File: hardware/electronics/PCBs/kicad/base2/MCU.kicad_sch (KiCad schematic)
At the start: 25 parts, among them J1 HEADER2, U1 W25Q16JVSSIQ, U6 RP2350A, Y1 ABM8-272-T3

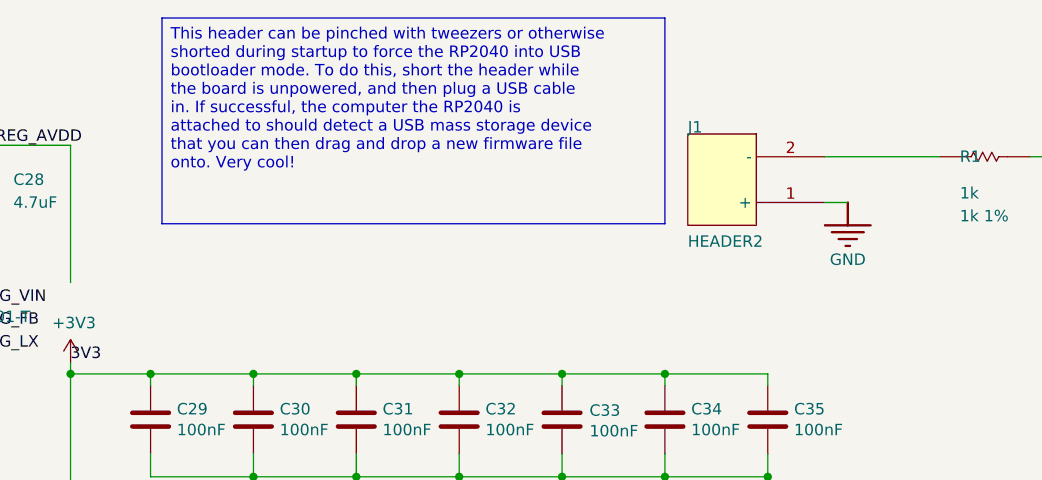
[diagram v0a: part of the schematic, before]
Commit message: Vertical neopixels
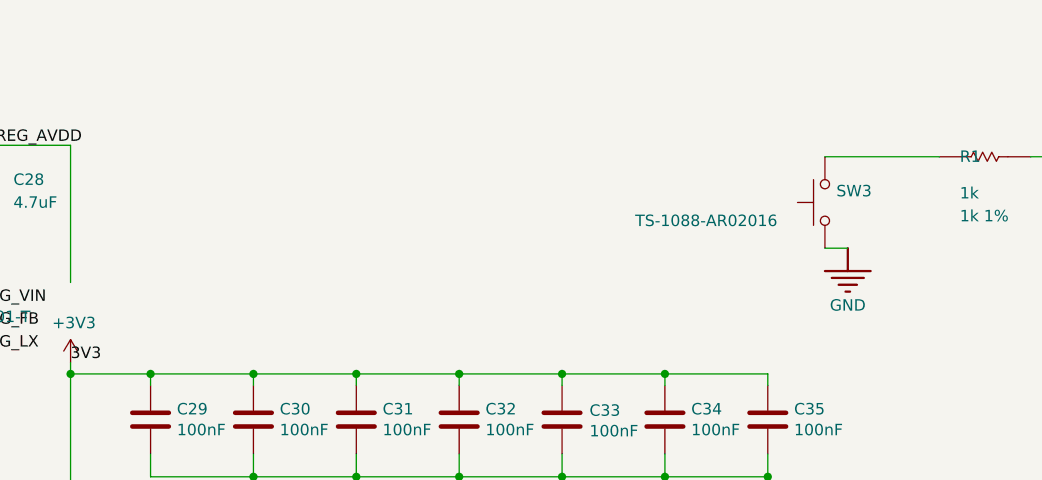
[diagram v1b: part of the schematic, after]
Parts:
- removed J1: HEADER2, 2x1, symbol Connectors:MCU_2_HEADER2_Connectors.SchLib
- added SW3: TS-1088-AR02016, Button_Switch_SMD:SW_SPST_TS-1088-xR020, symbol Switch:SW_Push
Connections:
- net GND: now also SW3.1
- net at R1.1: now also SW3.2
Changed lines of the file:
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@@
-		)
-	)
-	(text_box "This header can be pinched with tweezers or otherwise shorted during startup to force the RP2040 into USB bootloader mode. To do this, short the header while the board is unpowered, and then plug a USB cable in. If successful, the computer the RP2040 is attached to should detect a USB mass storage device that you can then drag and drop a new firmware file onto. Very cool!"
-		(exclude_from_sim no)
-		(at 167.64 65.8622 0)
-		(size -55.88 22.86)
-		(margins 0.9525 0.9525 0.9525 0.9525)
-		(stroke
-			(width 0)
-			(type default)
-			(color 0 0 0 1)
-		)
-		(fill
-			(type color)
-			(color 255 255 255 1)
-		)
-		(effects
-			(font
-				(size 1.27 1.27)
-			)
-			(justify left top)
 		)
 	)
@@
 	(wire
 		(pts
-			(xy 187.96 86.36) (xy 185.42 86.36)
+			(xy 187.96 91.44) (xy 185.42 91.44)
 		)
 		(stroke
@@
 	)
 	(symbol
+		(lib_id "Switch:SW_Push")
+		(at 185.42 86.36 90)
+		(unit 1)
+		(body_style 1)
+		(exclude_from_sim no)
+		(in_bom yes)
+		(on_board yes)
+		(in_pos_files yes)
+		(dnp no)
+		(property "Reference" "SW3"
+			(at 186.69 85.0899 90)
+			(show_name no)
+			(do_not_autoplace no)
+			(effects
+				(font
+					(size 1.27 1.27)
+				)
+				(justify right)
+			)
+		)
+		(property "Value" "TS-1088-AR02016"
+			(at 164.338 88.392 90)
+			(show_name no)
+			(do_not_autoplace no)
+			(effects
+				(font
+					(size 1.27 1.27)
+				)
+				(justify right)
+			)
+		)
+		(property "Footprint" "Button_Switch_SMD:SW_SPST_TS-1088-xR020"
+			(at 180.34 86.36 0)
+			(hide yes)
+			(show_name no)
+			(do_not_autoplace no)
+			(effects
+				(font
+					(size 1.27 1.27)
+				)
+			)
+		)
+		(property "Datasheet" ""
+			(at 180.34 86.36 0)
+			(hide yes)
+			(show_name no)
+			(do_not_autoplace no)
+			(effects
+				(font
+					(size 1.27 1.27)
+				)
+			)
+		)
+		(property "Description" "Push button switch, generic, two pins"
+			(at 185.42 86.36 0)
+			(hide yes)
+			(show_name no)
+			(do_not_autoplace no)
+			(effects
+				(font
+					(size 1.27 1.27)
+				)
+			)
+		)
+		(pin "1"
+		)
+		(pin "2"
+		)
+		(instances
+			(project "Base"
+				(path "/d0aa5c71-a42d-40bb-b9da-a8c48d59eca1/85f7b59c-4fd1-4617-9fbd-1127d31d6d70"
+					(reference "SW3")
+					(unit 1)
+				)
+			)
+		)
+	)
+	(symbol
 		(lib_id "Device:R")
 		(at 80.01 80.01 90)
@@
 	(symbol
 		(lib_id "Base-altium-import:GND_POWER_GROUND")
-		(at 187.96 86.36 0)
+		(at 187.96 91.44 0)
 		(unit 1)
 		(body_style 1)
@@
 		(dnp no)
 		(property "Reference" "#PWR012"
-			(at 187.96 86.36 0)
+			(at 187.96 91.44 0)
 			(hide yes)
 			(show_name no)
@@
 		)
 		(property "Value" "GND"
-			(at 187.96 92.71 0)
+			(at 187.96 97.79 0)
 			(show_name no)
 			(do_not_autoplace no)
@@
 		)
 		(property "Footprint" ""
-			(at 187.96 86.36 0)
+			(at 187.96 91.44 0)
 			(show_name no)
 			(do_not_autoplace no)
@@
 		)
 		(property "Datasheet" ""
-			(at 187.96 86.36 0)
+			(at 187.96 91.44 0)
 			(show_name no)
 			(do_not_autoplace no)
@@
 		)
 		(property "Description" ""
-			(at 187.96 86.36 0)
+			(at 187.96 91.44 0)
 			(show_name no)
 			(do_not_autoplace no)
@@
 					(unit 1)
 				)
-			)
-		)
-	)
-	(symbol
-		(lib_id "Connectors:MCU_2_HEADER2_Connectors.SchLib")
-		(at 175.26 83.82 270)
-		(unit 1)
-		(body_style 1)
-		(exclude_from_sim no)
-		(in_bom yes)
-		(on_board yes)
-		(in_pos_files yes)
-		(dnp no)
-		(property "Reference" "J1"
-			(at 170.18 78.74 90)
-			(show_name no)
-			(do_not_autoplace no)
-			(effects
-				(font
-					(size 1.27 1.27)
-				)
-				(justify left bottom)
-			)
-		)
-		(property "Value" "HEADER2"
-			(at 170.18 91.44 90)
-			(show_name no)
-			(do_not_autoplace no)
-			(effects
-				(font
-					(size 1.27 1.27)
-				)
-				(justify left bottom)
-			)
-		)
-		(property "Footprint" "2x1"
-			(at 175.26 83.82 0)
-			(hide yes)
-			(show_name no)
-			(do_not_autoplace no)
-			(effects
-				(font
-					(size 1.27 1.27)
-				)
-			)
-		)
-		(property "Datasheet" ""
-			(at 175.26 83.82 0)
-			(hide yes)
-			(show_name no)
-			(do_not_autoplace no)
-			(effects
-				(font
-					(size 1.27 1.27)
-				)
-			)
-		)
-		(property "Description" "2-pin 0.100\" header"
-			(at 175.26 83.82 0)
-			(hide yes)
-			(show_name no)
-			(do_not_autoplace no)
-			(effects
-				(font
-					(size 1.27 1.27)
-				)
-			)
-		)
-		(property "SUPPLIER 1" "Mouser"
-			(at 170.18 78.74 90)
-			(hide yes)
-			(show_name no)
-			(do_not_autoplace no)
-			(effects
-				(font
-					(size 1.27 1.27)
-				)
-				(justify left bottom)
-			)
-		)
-		(property "SUPPLIER PART NUMBER 1" "855-M20-9990245"
-			(at 170.18 78.74 90)
-			(hide yes)
-			(show_name no)
-			(do_not_autoplace no)
-			(effects
-				(font
-					(size 1.27 1.27)
-				)
-				(justify left bottom)
-			)
-		)
-		(property "SUPPLIER 2" "Digi-Key"
-			(at 170.18 78.74 90)
-			(hide yes)
-			(show_name no)
-			(do_not_autoplace no)
-			(effects
-				(font
-					(size 1.27 1.27)
-				)
-				(justify left bottom)
-			)
-		)
-		(property "SUPPLIER PART NUMBER 2" "952-2261-ND"
-			(at 170.18 78.74 90)
-			(hide yes)
-			(show_name no)
-			(do_not_autoplace no)
-			(effects
-				(font
-					(size 1.27 1.27)
-				)
-				(justify left bottom)
-			)
-		)
-		(pin "1"
-		)
-		(pin "2"
-		)
-		(instances
-			(project "Base"
-				(path "/d0aa5c71-a42d-40bb-b9da-a8c48d59eca1/85f7b59c-4fd1-4617-9fbd-1127d31d6d70"
-					(reference "J1")
-					(unit 1)
-				)
